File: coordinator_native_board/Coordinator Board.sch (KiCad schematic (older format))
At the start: 19 parts, among them P1 POWER, P10 Mounting Hole, P11 Mounting Hole, P12 Mounting Hole, P13 Mounting Hole, P3 Peripheral, P4 SERIAL, P5 PGRM, SW1 Switch_SPDT_x2, U1 LM3671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

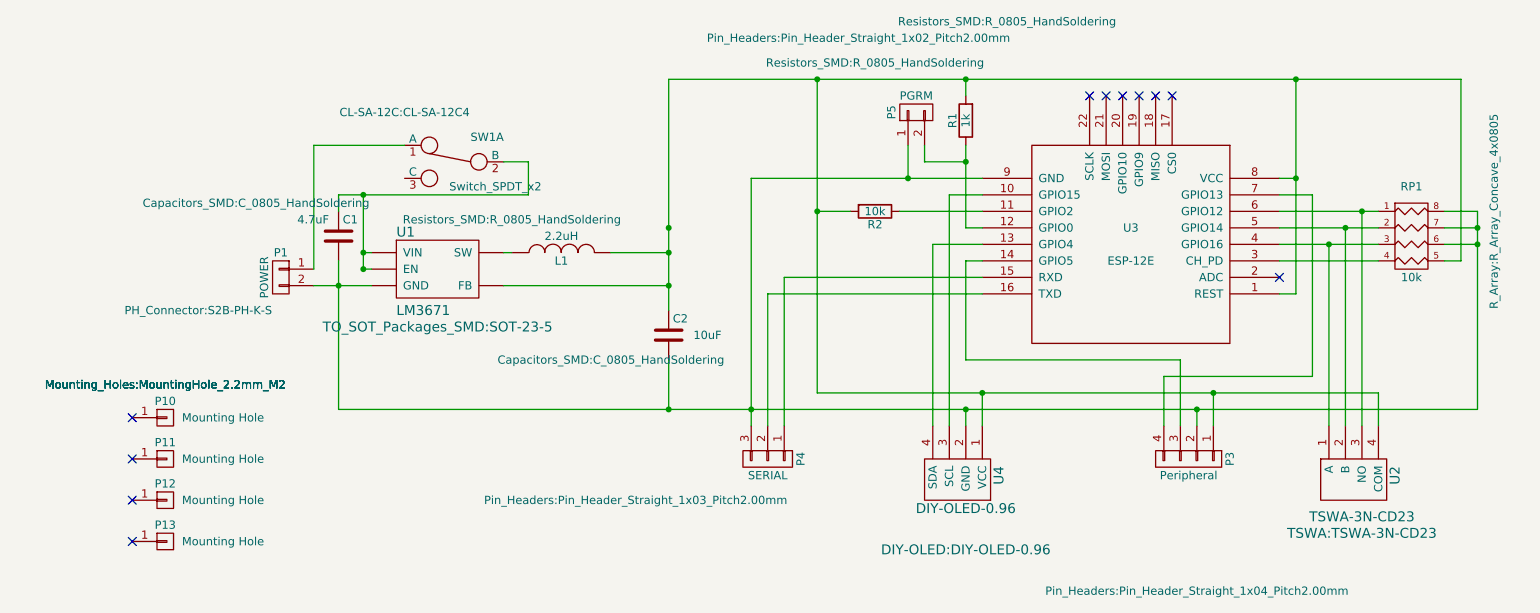
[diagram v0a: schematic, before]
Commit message: Reworked coordinator to use a generic rotary encoder
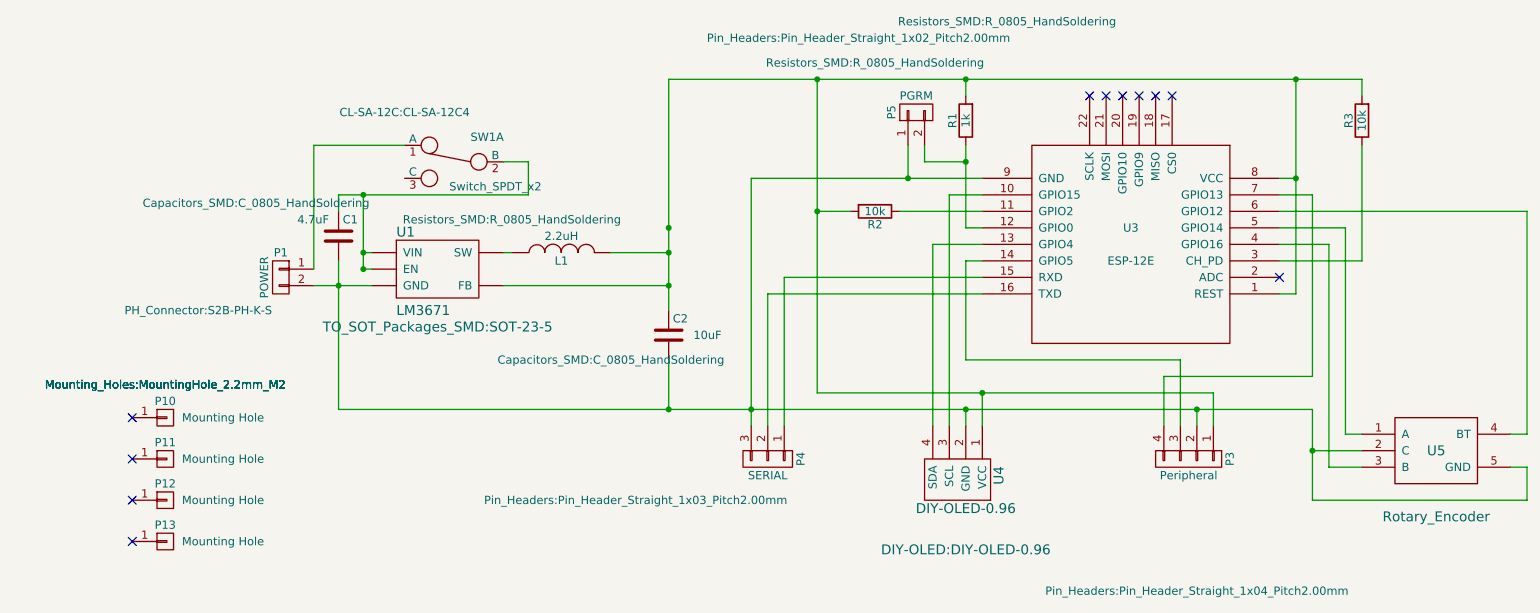
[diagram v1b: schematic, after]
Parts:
- removed RP1: 10k, R_Array:R_Array_Concave_4x0805, symbol R_PACK4
- removed U2: TSWA-3N-CD23, TSWA:TSWA-3N-CD23, symbol TSWA-3N-CD23
- added R3: 10k, symbol R
- added U5: Rotary_Encoder, symbol Rotary_Encoder
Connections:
- net at C1.2, C2.2, P1.2 (P2)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: now also U5.2 (C), U5.5 (GND)
- net at C2.1, L1.2, P3.1 (P1)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: now also R3.2
- net at U3.3 (CH_PD): now also R3.1
- net at U3.4 (GPIO16): now also U5.3 (B)
- net at U3.5 (GPIO14): now also U5.1 (A)
- net at U3.6 (GPIO12): now also U5.4 (BT)
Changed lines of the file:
@@
 LIBS:DIY-OLED
 LIBS:TSWA
+LIBS:Rotary_Encoder
 LIBS:Coordinator Board-cache
 EELAYER 25 0
@@
 $EndComp
 $Comp
-L R_PACK4 RP1
-U 1 1 5897D990
-P 9350 3600
-F 0 "RP1" H 9350 4100 50  0000 C CNN
-F 1 "10k" H 9350 3550 50  0000 C CNN
-F 2 "R_Array:R_Array_Concave_4x0805" V 9850 3950 50  0000 C CNN
-F 3 "" H 9350 3600 50  0000 C CNN
-	1    9350 3600
-	1    0    0    -1
-$EndComp
-$Comp
 L DIY-OLED-0.96 U4
 U 1 1 5898EB2B
@@
 NoConn ~ 1600 5000
 NoConn ~ 1600 5250
-$Comp
-L TSWA-3N-CD23 U2
-U 1 1 5897DDE5
-P 9050 4950
-F 0 "U2" V 9250 4850 60  0000 C CNN
-F 1 "TSWA-3N-CD23" H 9050 5100 60  0000 C CNN
-F 2 "TSWA:TSWA-3N-CD23" H 9050 5200 60  0000 C CNN
-F 3 "" H 9050 4950 60  0000 C CNN
-	1    9050 4950
-	1    0    0    1
-$EndComp
 Wire Wire Line
 	2700 3600 2700 2850
@@
 	3850 2950 4000 2950
 Wire Wire Line
-	3000 3150 3000 3600
+	3000 3150 3000 3500
+Wire Wire Line
+	3000 3500 3000 3600
 Wire Wire Line
 	3000 3500 3050 3500
 Connection ~ 3000 3500
 Wire Wire Line
-	2700 3700 3050 3700
-Wire Wire Line
-	2850 3550 2850 4450
-Wire Wire Line
-	2850 4450 9750 4450
+	2700 3700 2850 3700
+Wire Wire Line
+	2850 3700 3050 3700
+Wire Wire Line
+	2850 3550 2850 3700
+Wire Wire Line
+	2850 3700 2850 4450
+Wire Wire Line
+	2850 4450 4850 4450
+Wire Wire Line
+	4850 4450 5350 4450
+Wire Wire Line
+	5350 4450 6650 4450
+Wire Wire Line
+	6650 4450 8050 4450
+Wire Wire Line
+	8050 4450 8750 4450
 Connection ~ 2850 3700
 Wire Wire Line
 	3850 3500 3900 3500
 Wire Wire Line
-	4000 2950 4000 3150
-Wire Wire Line
-	4000 3150 2850 3150
+	4000 3150 4000 2950
+Wire Wire Line
+	2850 3150 3000 3150
+Wire Wire Line
+	3000 3150 4000 3150
 Wire Wire Line
 	2850 3150 2850 3250
 Connection ~ 3000 3150
 Wire Wire Line
-	4850 2450 4850 3850
+	4850 2450 4850 3350
+Wire Wire Line
+	4850 3350 4850 3500
+Wire Wire Line
+	4850 3500 4850 3700
+Wire Wire Line
+	4850 3700 4850 3850
 Wire Wire Line
 	3850 3700 4850 3700
@@
 Connection ~ 4850 3500
 Wire Wire Line
-	5350 3050 5350 4550
+	5350 3050 5350 4450
+Wire Wire Line
+	5350 4450 5350 4550
 Connection ~ 5350 4450
 Wire Wire Line
@@
 	8650 3750 8550 3750
 Wire Wire Line
-	4850 2450 9650 2450
+	4850 2450 5750 2450
+Wire Wire Line
+	5750 2450 6650 2450
+Wire Wire Line
+	6650 2450 8650 2450
+Wire Wire Line
+	8650 2450 9050 2450
 Connection ~ 8650 3050
 Connection ~ 4850 3350
@@
 Connection ~ 6650 2450
 Wire Wire Line
-	6650 2850 6650 3350
+	6650 2850 6650 2950
+Wire Wire Line
+	6650 2950 6650 3350
 Wire Wire Line
 	6300 2850 6300 3050
@@
 	5750 3250 5950 3250
 Wire Wire Line
-	5750 2450 5750 4350
+	5750 2450 5750 3250
+Wire Wire Line
+	5750 3250 5750 4350
 Connection ~ 5750 2450
 Wire Wire Line
-	5350 3050 6750 3050
+	5350 3050 6300 3050
+Wire Wire Line
+	6300 3050 6750 3050
 Wire Wire Line
 	6750 3250 6250 3250
 Wire Wire Line
-	8650 2450 8650 3750
+	8650 2450 8650 3050
+Wire Wire Line
+	8650 3050 8650 3750
 Wire Wire Line
 	8550 3050 8650 3050
 Wire Wire Line
-	9650 2450 9650 3550
-Wire Wire Line
-	9750 4450 9750 3250
-Connection ~ 9750 3350
-Connection ~ 9750 3450
-Wire Wire Line
-	8050 4550 8050 4450
-Connection ~ 8050 4450
-Wire Wire Line
-	5750 4350 9150 4350
+	8050 4450 8050 4550
+Wire Wire Line
+	5750 4350 6750 4350
+Wire Wire Line
+	6750 4350 8150 4350
 Connection ~ 5750 3250
 Wire Wire Line
@@
 Wire Wire Line
 	8750 4250 7850 4250
-Connection ~ 8150 4350
-Wire Wire Line
-	8850 3450 8850 4550
-Connection ~ 8850 3450
-Wire Wire Line
-	8950 3350 8950 4550
-Connection ~ 8950 3350
-Wire Wire Line
-	9050 3250 9050 4550
-Connection ~ 9050 3250
-Wire Wire Line
-	9150 4350 9150 4550
 Wire Wire Line
 	6450 3450 6750 3450
@@
 Wire Wire Line
 	6550 3150 6550 4550
-Wire Wire Line
-	8550 3250 9150 3250
-Wire Wire Line
-	8550 3350 9150 3350
-Wire Wire Line
-	8550 3450 9150 3450
-Wire Wire Line
-	8550 3550 9150 3550
-Wire Wire Line
-	9750 3250 9550 3250
-Wire Wire Line
-	9750 3350 9550 3350
-Wire Wire Line
-	9550 3450 9750 3450
-Wire Wire Line
-	9650 3550 9550 3550
 Wire Wire Line
 	6750 4550 6750 4350
@@
 	6650 4550 6650 4450
 Connection ~ 6650 4450
+$Comp
+L R R3
+U 1 1 58D3649D
+P 9050 2700
+F 0 "R3" V 9130 2700 50  0000 C CNN
+F 1 "10k" V 9050 2700 50  0000 C CNN
+F 2 "" V 8980 2700 50  0000 C CNN
+F 3 "" H 9050 2700 50  0000 C CNN
+	1    9050 2700
+	-1   0    0    1
+$EndComp
+$Comp
+L Rotary_Encoder U5
+U 1 1 58D36C2B
+P 9500 4850
+F 0 "U5" V 9350 4850 60  0000 C CNN
+F 1 "Rotary_Encoder" V 9750 4850 60  0000 C CNN
+F 2 "" H 9500 4850 60  0000 C CNN
+F 3 "" H 9500 4850 60  0000 C CNN
+	1    9500 4850
+	0    1    1    0
+$EndComp
+Wire Wire Line
+	9950 4600 10050 4600
+Wire Wire Line
+	10050 4600 10050 3250
+Wire Wire Line
+	10050 3250 8550 3250
+Wire Wire Line
+	8550 3450 8850 3450
+Wire Wire Line
+	8850 3450 8850 4800
+Wire Wire Line
+	8850 4800 9050 4800
+Wire Wire Line
+	8550 3350 8950 3350
+Wire Wire Line
+	8950 3350 8950 4600
+Wire Wire Line
+	8950 4600 9050 4600
+Wire Wire Line
+	9950 4800 10050 4800
+Wire Wire Line
+	10050 4800 10050 5000
+Wire Wire Line
+	8750 5000 10050 5000
+Wire Wire Line
+	8750 4450 8750 4700
+Wire Wire Line
+	8750 4700 8750 5000
+Connection ~ 8050 4450
+Wire Wire Line
+	9050 4700 8750 4700
+Connection ~ 8750 4700
+Wire Wire Line
+	8550 3550 9050 3550
+Wire Wire Line
+	9050 3550 9050 2850
+Wire Wire Line
+	9050 2450 9050 2550
 $EndSCHEMATC
